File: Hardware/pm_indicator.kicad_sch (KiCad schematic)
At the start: 4 parts, among them Q1 2N3904

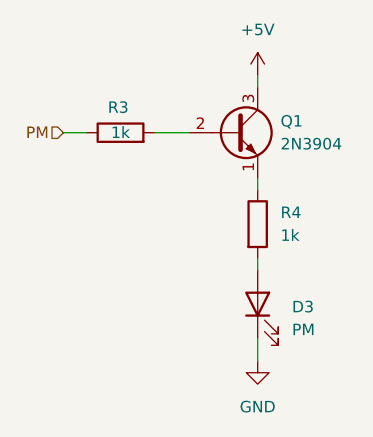
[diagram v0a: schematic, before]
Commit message: chore: Finilize circuit parity
Add colon LEDs
Reannotate reference designations
Update footprints

Signed-off-by: Joel Cranmer <42.joel.cranmer@gmail.com>
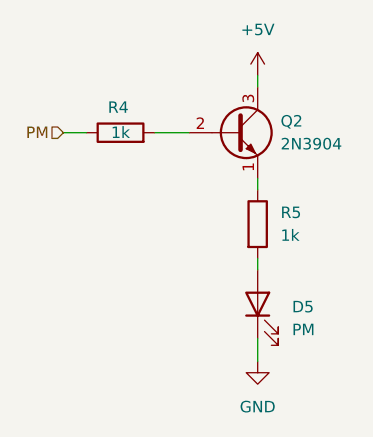
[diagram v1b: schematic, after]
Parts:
- R4: renamed from R3; footprint (none) -> Resistor_SMD:R_0603_1608Metric
- R5: renamed from R4; footprint (none) -> Resistor_SMD:R_0603_1608Metric
- renumbered D3 to D5, Q1 to Q2
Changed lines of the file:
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@@
 		(on_board yes)
 		(dnp no)
-		(property "Reference" "R3"
+		(property "Reference" "R4"
 			(at 82.296 65.786 90)
 			(effects
@@
 			)
 		)
-		(property "Footprint" ""
+		(property "Footprint" "Resistor_SMD:R_0603_1608Metric"
 			(at 82.55 70.358 90)
 			(effects
@@
 			(project "AC_Clock"
 				(path "/25ded3d7-7fc5-4a73-82e8-c02ba32fe53a/2905fac8-d818-4a72-9c6c-e2a6c6597572"
-					(reference "R3")
+					(reference "R4")
 					(unit 1)
 				)
@@
 		(dnp no)
 		(fields_autoplaced yes)
-		(property "Reference" "Q1"
+		(property "Reference" "Q2"
 			(at 100.33 67.3099 0)
 			(effects
@@
 			(project ""
 				(path "/25ded3d7-7fc5-4a73-82e8-c02ba32fe53a/2905fac8-d818-4a72-9c6c-e2a6c6597572"
-					(reference "Q1")
+					(reference "Q2")
 					(unit 1)
 				)
@@
 		(dnp no)
 		(fields_autoplaced yes)
-		(property "Reference" "R4"
+		(property "Reference" "R5"
 			(at 100.33 77.4699 0)
 			(effects
@@
 			)
 		)
-		(property "Footprint" ""
+		(property "Footprint" "Resistor_SMD:R_0603_1608Metric"
 			(at 96.012 78.74 90)
 			(effects
@@
 			(project ""
 				(path "/25ded3d7-7fc5-4a73-82e8-c02ba32fe53a/2905fac8-d818-4a72-9c6c-e2a6c6597572"
-					(reference "R4")
+					(reference "R5")
 					(unit 1)
 				)
@@
 		(dnp no)
 		(fields_autoplaced yes)
-		(property "Reference" "#PWR043"
+		(property "Reference" "#PWR045"
 			(at 97.79 66.04 0)
 			(effects
@@
 			(project "AC_Clock"
 				(path "/25ded3d7-7fc5-4a73-82e8-c02ba32fe53a/2905fac8-d818-4a72-9c6c-e2a6c6597572"
-					(reference "#PWR043")
+					(reference "#PWR045")
 					(unit 1)
 				)
@@
 		(dnp no)
 		(fields_autoplaced yes)
-		(property "Reference" "#PWR044"
+		(property "Reference" "#PWR046"
 			(at 97.79 100.33 0)
 			(effects
@@
 			(project "AC_Clock"
 				(path "/25ded3d7-7fc5-4a73-82e8-c02ba32fe53a/2905fac8-d818-4a72-9c6c-e2a6c6597572"
-					(reference "#PWR044")
+					(reference "#PWR046")
 					(unit 1)
 				)
@@
 		(dnp no)
 		(fields_autoplaced yes)
-		(property "Reference" "D3"
+		(property "Reference" "D5"
 			(at 101.6 87.9474 90)
 			(effects
@@
 			(project "AC_Clock"
 				(path "/25ded3d7-7fc5-4a73-82e8-c02ba32fe53a/2905fac8-d818-4a72-9c6c-e2a6c6597572"
-					(reference "D3")
-					(unit 1)
-				)
+					(reference "D5")
+					(unit 1)
+				)

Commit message: feat: Create new PCB layout (draft)
Signed-off-by: Joel Cranmer <42.joel.cranmer@gmail.com>
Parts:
- Q2: footprint Package_TO_SOT_THT:TO-92_Inline -> Package_TO_SOT_THT:TO-92_Inline_Wide
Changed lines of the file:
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@@
 			)
 		)
-		(property "Footprint" "Package_TO_SOT_THT:TO-92_Inline"
+		(property "Footprint" "Package_TO_SOT_THT:TO-92_Inline_Wide"
 			(at 100.33 70.485 0)
 			(effects
